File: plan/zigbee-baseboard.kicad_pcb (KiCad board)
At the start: 4 copper layers, 0 parts

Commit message: Initially update board from schematic
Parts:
- added AE1: 2450AT18A0100001E, Smarthome:Antenna_Johanson_2450AT18A0100001E, F.Cu at (128.1, 104.3)
- added C1: 2,3 pF, Capacitor_SMD:C_0201_0603Metric, F.Cu at (126.7, 98.1)
- added C101: 100 nF, Capacitor_SMD:C_0402_1005Metric, F.Cu at (126.9, 80.5)
- added C102: 10 µF, Capacitor_SMD:C_0603_1608Metric, F.Cu at (130.4, 86.0)
- added C103: 4,7 µF, Capacitor_SMD:C_0603_1608Metric, F.Cu at (130.4, 88.5)
- added C104: 1 µF, Capacitor_SMD:C_0402_1005Metric, F.Cu at (126.9, 82.5)
- added C105: 1 µF, Capacitor_SMD:C_0402_1005Metric, F.Cu at (126.9, 84.4)
- added C106: 1 µF, Capacitor_SMD:C_0402_1005Metric, F.Cu at (126.9, 86.4)
- added C107: 18 pF, Capacitor_SMD:C_0201_0603Metric, F.Cu at (129.6, 80.4)
- added C108: 0,5 pF, Capacitor_SMD:C_0201_0603Metric, F.Cu at (129.6, 82.1)
- added C109: 1 µF, Capacitor_SMD:C_0402_1005Metric, F.Cu at (126.9, 88.4)
- added C110: 1 µF, Capacitor_SMD:C_0402_1005Metric, F.Cu at (126.9, 90.3)
- added C111: 100 nF, Capacitor_SMD:C_0402_1005Metric, F.Cu at (126.9, 92.3)
- added C112: 100 nF, Capacitor_SMD:C_0402_1005Metric, F.Cu at (126.9, 94.3)
- added C2: 1,6 pF, Capacitor_SMD:C_0201_0603Metric, F.Cu at (126.7, 99.9)
- added C3: 0,3 pF, Capacitor_SMD:C_0201_0603Metric, F.Cu at (126.7, 101.6)
- added C4: TUNE, Capacitor_SMD:C_0201_0603Metric, F.Cu at (129.2, 98.1)
- added C5: TUNE, Capacitor_SMD:C_0201_0603Metric, F.Cu at (129.2, 99.9)
- added CC1: 0 Ω, Resistor_SMD:R_0201_0603Metric, F.Cu at (129.2, 101.6)
- added D1: APT1608LZGCK, LED_SMD:LED_0603_1608Metric, F.Cu at (143.0, 101.5)
- added FB101: 70 Ω @ 100 MHz, Inductor_SMD:L_0201_0603Metric, F.Cu at (129.6, 83.9)
- added J1: Debug_SWD_Pogo_2x3, Smarthome:Debug_SWD_Pogo_2x3_P2.00mm, F.Cu at (138.5, 102.6)
- added J2: EFR32MG24_Core_Expansion_2x6, Smarthome:Module_EFR32MG24_Core_Castellated_2x6_PTH_P2.54mm, F.Cu at (136.8, 87.2)
- added L1: 2,9 nH, Inductor_SMD:L_0201_0603Metric, F.Cu at (131.6, 98.1)
- added L101: DFE2HCAH2R2MJ0, Smarthome:Inductor_Murata_DFE2HCAH_2520, F.Cu at (130.6, 91.6)
- added L2: 1,2 nH, Inductor_SMD:L_0201_0603Metric, F.Cu at (131.6, 99.9)
- added L3: TUNE, Inductor_SMD:L_0201_0603Metric, F.Cu at (131.6, 101.6)
- added R1: 2.2 kΩ, 1%, Resistor_SMD:R_0402_1005Metric, F.Cu at (142.4, 103.8)
- added R101: 0 Ω, Resistor_SMD:R_0402_1005Metric, F.Cu at (132.3, 80.5)
- added R102: 0 Ω, Resistor_SMD:R_0402_1005Metric, F.Cu at (132.3, 82.5)
- added SW1: EVPBB2A9B000, Smarthome:Button_Panasonic_EVPBB_2.6x1.6mm, F.Cu at (143.3, 98.7)
- added TP1: GPIO_SolderPad, Smarthome:GPIO_SolderPad_D1.0mm_Bottom, F.Cu at (155.1, 80.8)
- added TP10: GPIO_SolderPad, Smarthome:GPIO_SolderPad_D1.0mm_Bottom, F.Cu at (157.7, 88.4)
- added TP11: GPIO_SolderPad, Smarthome:GPIO_SolderPad_D1.0mm_Bottom, F.Cu at (157.7, 91.0)
- added TP12: GPIO_SolderPad, Smarthome:GPIO_SolderPad_D1.0mm_Bottom, F.Cu at (157.7, 93.5)
- added TP13: GPIO_SolderPad, Smarthome:GPIO_SolderPad_D1.0mm_Bottom, F.Cu at (160.2, 80.8)
- added TP14: GPIO_SolderPad, Smarthome:GPIO_SolderPad_D1.0mm_Bottom, F.Cu at (160.2, 83.3)
- added TP15: GPIO_SolderPad, Smarthome:GPIO_SolderPad_D1.0mm_Bottom, F.Cu at (160.2, 85.9)
- added TP16: GPIO_SolderPad, Smarthome:GPIO_SolderPad_D1.0mm_Bottom, F.Cu at (160.2, 88.4)
- added TP17: GPIO_SolderPad, Smarthome:GPIO_SolderPad_D1.0mm_Bottom, F.Cu at (160.2, 91.0)
- added TP18: GPIO_SolderPad, Smarthome:GPIO_SolderPad_D1.0mm_Bottom, F.Cu at (160.2, 93.5)
- added TP19: GPIO_SolderPad, Smarthome:GPIO_SolderPad_D1.0mm_Bottom, F.Cu at (162.8, 80.8)
- added TP2: GPIO_SolderPad, Smarthome:GPIO_SolderPad_D1.0mm_Bottom, F.Cu at (155.1, 83.3)
- added TP20: GPIO_SolderPad, Smarthome:GPIO_SolderPad_D1.0mm_Bottom, F.Cu at (162.8, 83.3)
- added TP21: GPIO_SolderPad, Smarthome:GPIO_SolderPad_D1.0mm_Bottom, F.Cu at (162.8, 85.9)
- added TP22: GPIO_SolderPad, Smarthome:GPIO_SolderPad_D1.0mm_Bottom, F.Cu at (162.8, 88.4)
- added TP3: GPIO_SolderPad, Smarthome:GPIO_SolderPad_D1.0mm_Bottom, F.Cu at (155.1, 85.9)
- added TP4: GPIO_SolderPad, Smarthome:GPIO_SolderPad_D1.0mm_Bottom, F.Cu at (155.1, 88.4)
- added TP5: GPIO_SolderPad, Smarthome:GPIO_SolderPad_D1.0mm_Bottom, F.Cu at (155.1, 91.0)
- added TP6: GPIO_SolderPad, Smarthome:GPIO_SolderPad_D1.0mm_Bottom, F.Cu at (155.1, 93.5)
- added TP7: GPIO_SolderPad, Smarthome:GPIO_SolderPad_D1.0mm_Bottom, F.Cu at (157.7, 80.8)
- added TP8: GPIO_SolderPad, Smarthome:GPIO_SolderPad_D1.0mm_Bottom, F.Cu at (157.7, 83.3)
- added TP9: GPIO_SolderPad, Smarthome:GPIO_SolderPad_D1.0mm_Bottom, F.Cu at (157.7, 85.9)
- added U1: EFR32MG24B020F1536IM48-B, Smarthome:QFN-48-1EP_6x6mm_P0.4mm_EFR32MG24, F.Cu at (152.0, 101.1)
- added Y1: XTL501250-S315-038, Smarthome:Crystal_Siward_XTL501250_2.0x1.6mm, F.Cu at (149.6, 107.1)

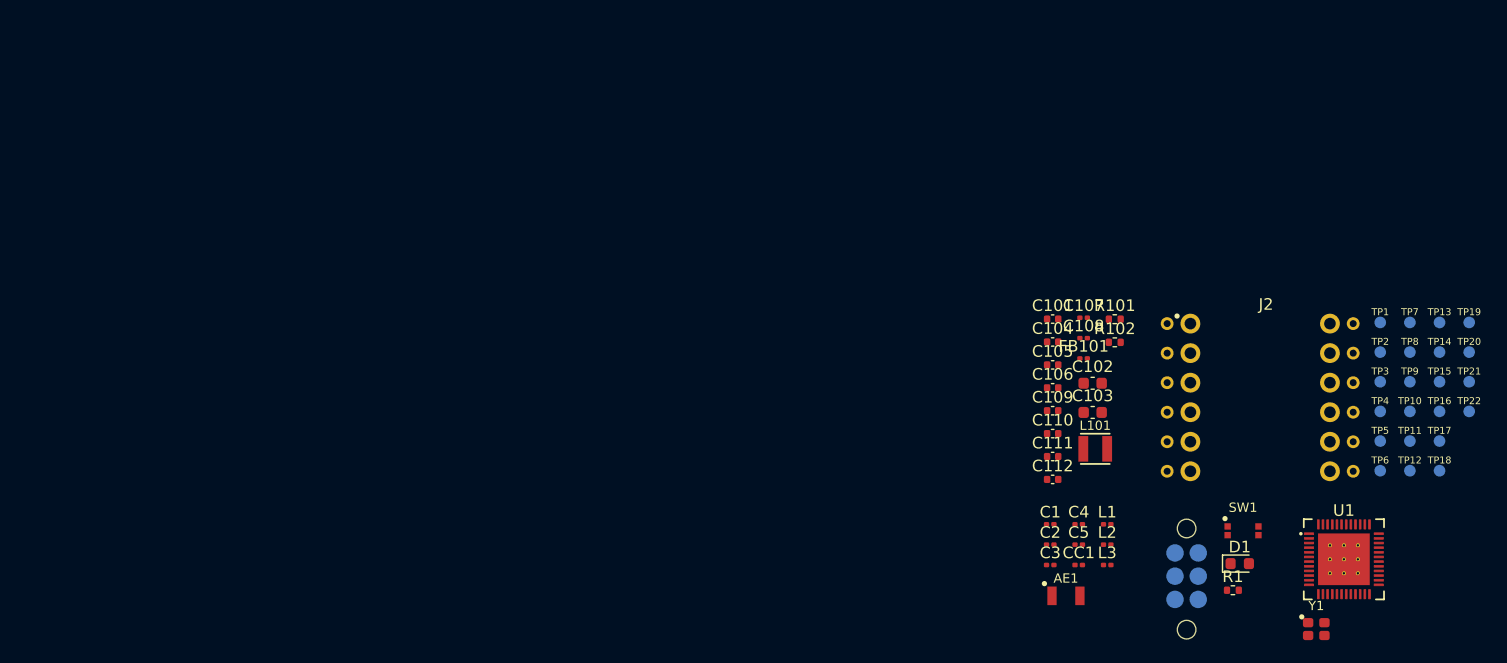
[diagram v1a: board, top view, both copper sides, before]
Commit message: First raw placement of RF-Block
- RF-Matching-Network
- Antenna-Tuning-Network
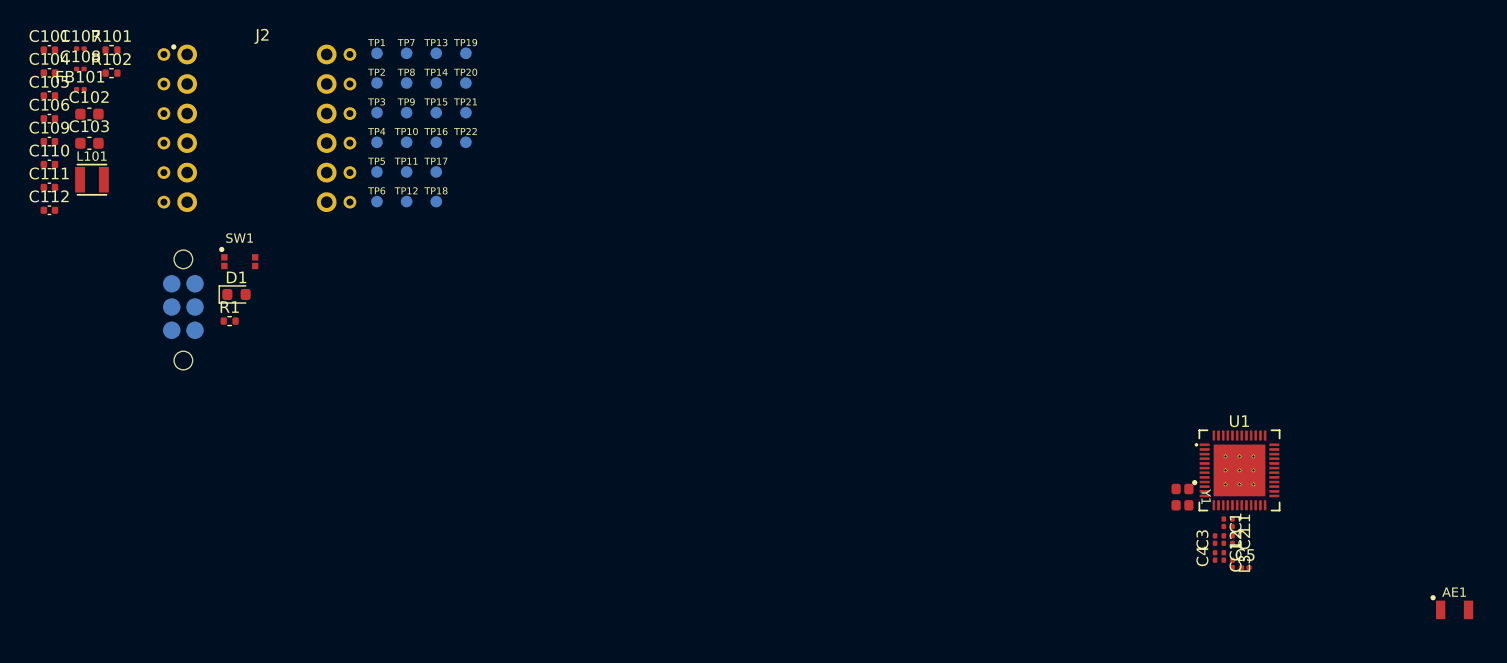
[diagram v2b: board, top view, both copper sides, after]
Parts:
- moved J1 89.3 mm to (52.2, 79.5)
- moved TP13 89.3 mm to (73.9, 57.6)
- moved TP14 89.3 mm to (73.9, 60.2)
- moved TP15 89.3 mm to (73.9, 62.7)
- moved TP16 89.3 mm to (73.9, 65.3)
- moved TP17 89.3 mm to (73.9, 67.8)
- moved TP18 89.3 mm to (73.9, 70.4)
- moved C101 89.3 mm to (40.7, 57.3)
- moved C102 89.3 mm to (44.1, 62.9)
- moved C103 89.3 mm to (44.1, 65.4)
- moved C104 89.3 mm to (40.7, 59.3)
- moved C105 89.3 mm to (40.7, 61.3)
- moved C106 89.3 mm to (40.7, 63.2)
- moved C107 89.3 mm to (43.3, 57.2)
- moved C108 89.3 mm to (43.3, 59.0)
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
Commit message: First raw placement of Power-Section
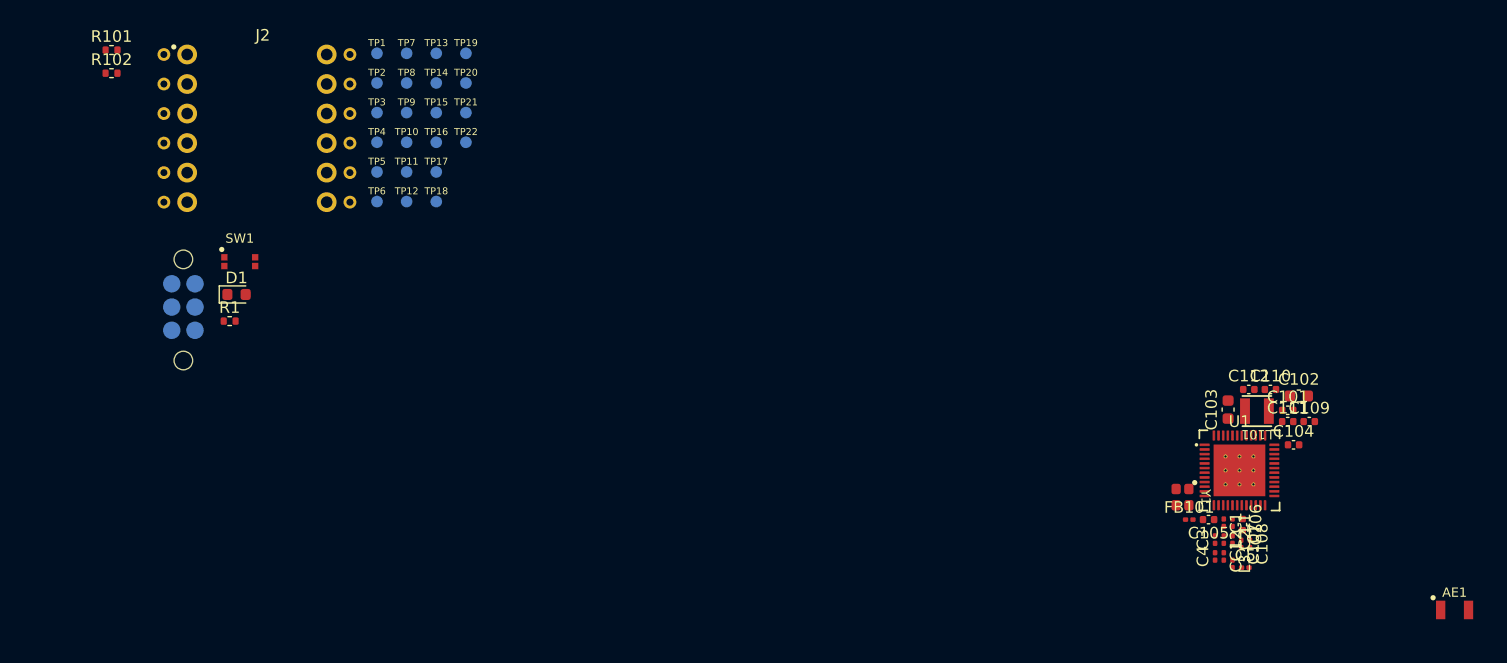
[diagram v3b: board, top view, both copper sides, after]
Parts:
- moved C104 111.7 mm to (147.7, 91.3)
- moved C109 111.0 mm to (149.0, 89.3)
- moved C101 110.9 mm to (147.2, 88.3)
- moved C108 108.6 mm to (143.9, 99.8), turned to -90 degrees
- moved C107 108.5 mm to (143.2, 99.8), turned to -90 degrees
- moved C111 108.4 mm to (147.2, 89.3)
- moved C106 108.4 mm to (143.2, 98.2), turned to -90 degrees
- moved C102 106.8 mm to (148.1, 87.1)
- moved C110 106.8 mm to (145.7, 86.5)
- moved C105 106.1 mm to (140.3, 97.7), turned to 180 degrees
- moved C112 104.3 mm to (143.8, 86.5)
- moved FB101 102.3 mm to (138.7, 97.7)
- moved L101 102.1 mm to (144.5, 88.4), turned to 180 degrees
- moved C103 100.6 mm to (142.0, 88.3), turned to 90 degrees

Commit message: Place antenna
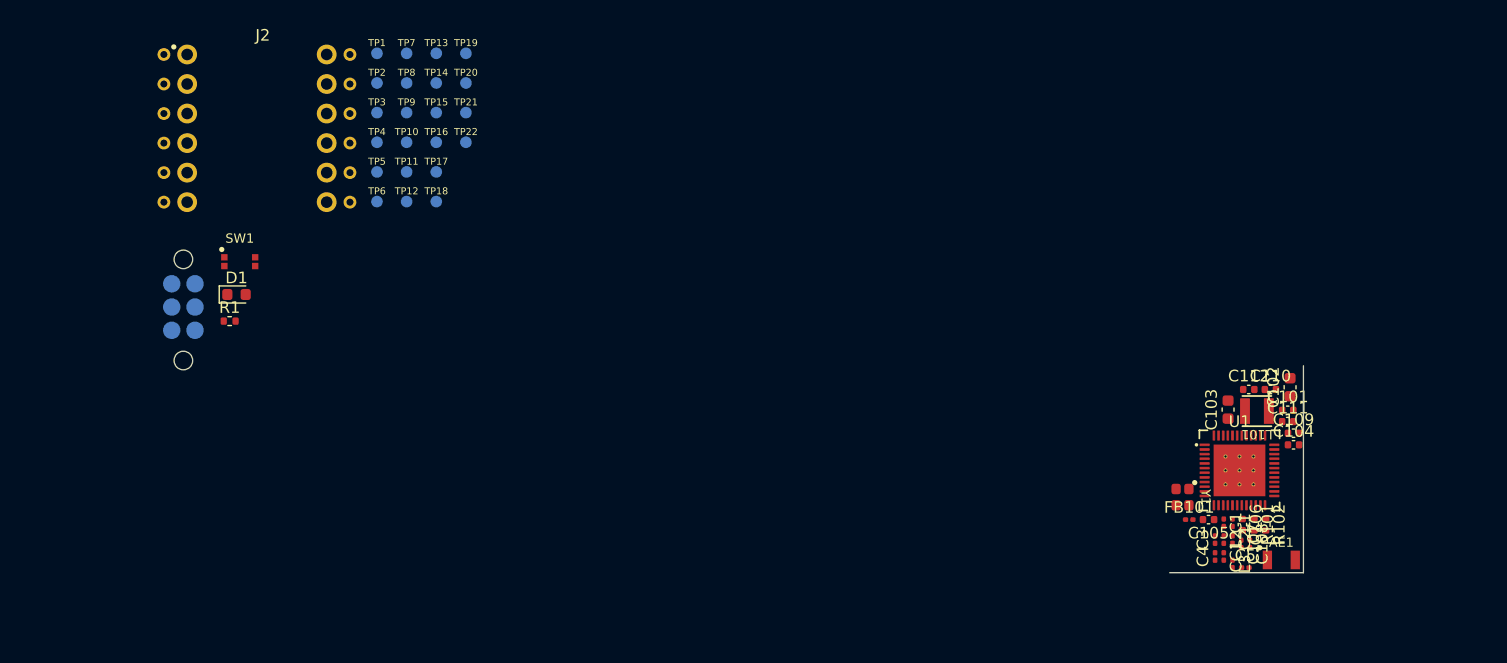
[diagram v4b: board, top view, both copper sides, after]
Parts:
- moved R102 106.6 mm to (145.2, 98.2), turned to -90 degrees
- moved R101 106.4 mm to (144.2, 98.2), turned to -90 degrees
- moved AE1 15.5 mm to (146.6, 101.2)
- moved C109 1.68 mm to (147.7, 90.3)
- moved C102 1.06 mm to (147.3, 86.3), turned to 90 degrees
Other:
- board outline added: 11.5 x 17.8 mm
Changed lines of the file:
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@@
 		(capping no)
 		(filling no)
-		(zone_defaults)
 		(pcbplotparams
 			(layerselection 0x00000000_00000000_55555555_5755f5ff)
@@
 	)
 	(footprint "Capacitor_SMD:C_0402_1005Metric"
+		(locked yes)
 		(layer "F.Cu")
 		(at 147.65 91.3)
@@
 	(footprint "Resistor_SMD:R_0402_1005Metric"
 		(layer "F.Cu")
-		(at 45.995 59.34)
+		(at 145.25 98.16 -90)
 		(descr "Resistor SMD 0402 (1005 Metric), square (rectangular) end terminal, IPC-7351 nominal, (Body size source: IPC-SM-782 page 72, https://www.pcb-3d.com/wordpress/wp-content/uploads/ipc-sm-782a_amendment_1_and_2.pdf)")
 		(tags "resistor")
 		(property "Reference" "R102"
-			(at 0 -1.17 0)
+			(at 0 -1.17 90)
 			(layer "F.SilkS")
 			(effects
@@
 		)
 		(property "Value" "0 Ω"
-			(at 0 1.17 0)
+			(at 0 1.17 90)
 			(layer "F.Fab")
 			(effects
@@
 		)
 		(property "Datasheet" ""
-			(at 0 0 0)
+			(at 0 0 90)
 			(layer "F.Fab")
 			(hide yes)
@@
 		)
 		(property "Description" "Resistor"
-			(at 0 0 0)
+			(at 0 0 90)
 			(layer "F.Fab")
 			(hide yes)
@@
 		)
 		(property "KiLib_Generator" "SMD_2terminal_chip_molded"
-			(at 0 0 0)
+			(at 0 0 90)
 			(layer "F.SilkS")
 			(hide yes)
@@
 		(duplicate_pad_numbers_are_jumpers no)
 		(fp_line
-			(start -0.153641 -0.38)
-			(end 0.153641 -0.38)
+			(start -0.153641 0.38)
+			(end 0.153641 0.38)
 			(stroke
 				(width 0.12)
@@
 		)
 		(fp_line
-			(start -0.153641 0.38)
-			(end 0.153641 0.38)
+			(start -0.153641 -0.38)
+			(end 0.153641 -0.38)
 			(stroke
 				(width 0.12)
@@
 		)
 		(fp_text user "${REFERENCE}"
-			(at 0 0 0)
+			(at 0 0 90)
 			(layer "F.Fab")
 			(effects
@@
 		)
 		(pad "1" smd roundrect
-			(at -0.51 0)
+			(at -0.51 0 270)
 			(size 0.54 0.64)
 			(layers "F.Cu" "F.Mask" "F.Paste")
@@
 		)
 		(pad "2" smd roundrect
-			(at 0.51 0)
+			(at 0.51 0 270)
 			(size 0.54 0.64)
 			(layers "F.Cu" "F.Mask" "F.Paste")
@@
 		(locked yes)
 		(layer "F.Cu")
-		(at 148.1 87.1)
+		(at 147.35 86.35 90)
 		(descr "Capacitor SMD 0603 (1608 Metric), square (rectangular) end terminal, IPC-7351 nominal, (Body size source: IPC-SM-782 page 76, https://www.pcb-3d.com/wordpress/wp-content/uploads/ipc-sm-782a_amendment_1_and_2.pdf)")
 		(tags "capacitor")
 		(property "Reference" "C102"
-			(at 0 -1.43 0)
+			(at 0 -1.43 90)
 			(layer "F.SilkS")
 			(effects
@@
 		)
 		(property "Value" "10 µF"
-			(at 0 1.43 0)
+			(at 0 1.43 90)
 			(layer "F.Fab")
 			(effects
@@
 		)
 		(property "Datasheet" ""
-			(at 0 0 0)
+			(at 0 0 90)
 			(layer "F.Fab")
 			(hide yes)
@@
 		)
 		(property "Description" "Polarized capacitor"
-			(at 0 0 0)
+			(at 0 0 90)
 			(layer "F.Fab")
 			(hide yes)
@@
 		)
 		(property "KiLib_Generator" "SMD_2terminal_chip_molded"
-			(at 0 0 0)
+			(at 0 0 90)
 			(layer "F.SilkS")
 			(hide yes)
@@
 		)
 		(fp_text user "${REFERENCE}"
-			(at 0 0 0)
+			(at 0 0 90)
 			(layer "F.Fab")
 			(effects
@@
 		)
 		(pad "1" smd roundrect
-			(at -0.775 0)
+			(at -0.775 0 90)
 			(size 0.9 0.95)
 			(layers "F.Cu" "F.Mask" "F.Paste")
@@
 		)
 		(pad "2" smd roundrect
-			(at 0.775 0)
+			(at 0.775 0 90)
 			(size 0.9 0.95)
 			(layers "F.Cu" "F.Mask" "F.Paste")
@@
 	(footprint "Smarthome:Antenna_Johanson_2450AT18A0100001E"
 		(layer "F.Cu")
-		(at 161.5 105.5)
+		(at 146.6 101.2)
 		(property "Reference" "AE1"
 			(at 0 -1.5 0)
@@
 		(locked yes)
 		(layer "F.Cu")
-		(at 149 89.3)
+		(at 147.65 90.3)
 		(descr "Capacitor SMD 0402 (1005 Metric), square (rectangular) end terminal, IPC-7351 nominal, (Body size source: IPC-SM-782 page 76, https://www.pcb-3d.com/wordpress/wp-content/uploads/ipc-sm-782a_amendment_1_and_2.pdf)")
 		(tags "capacitor")
@@
 	(footprint "Resistor_SMD:R_0402_1005Metric"
 		(layer "F.Cu")
-		(at 45.995 57.35)
+		(at 144.25 98.16 -90)
 		(descr "Resistor SMD 0402 (1005 Metric), square (rectangular) end terminal, IPC-7351 nominal, (Body size source: IPC-SM-782 page 72, https://www.pcb-3d.com/wordpress/wp-content/uploads/ipc-sm-782a_amendment_1_and_2.pdf)")
 		(tags "resistor")
 		(property "Reference" "R101"
-			(at 0 -1.17 0)
+			(at 0 -1.17 90)
 			(layer "F.SilkS")
 			(effects
@@
 		)
 		(property "Value" "0 Ω"
-			(at 0 1.17 0)
+			(at 0 1.17 90)
 			(layer "F.Fab")
 			(effects
@@
 		)
 		(property "Datasheet" ""
-			(at 0 0 0)
+			(at 0 0 90)
 			(layer "F.Fab")
 			(hide yes)
@@
 		)
 		(property "Description" "Resistor"
-			(at 0 0 0)
+			(at 0 0 90)
 			(layer "F.Fab")
 			(hide yes)
@@
 		)
 		(property "KiLib_Generator" "SMD_2terminal_chip_molded"
-			(at 0 0 0)
+			(at 0 0 90)
 			(layer "F.SilkS")
 			(hide yes)
@@
 		(duplicate_pad_numbers_are_jumpers no)
 		(fp_line
-			(start -0.153641 -0.38)
-			(end 0.153641 -0.38)
+			(start -0.153641 0.38)
+			(end 0.153641 0.38)
 			(stroke
 				(width 0.12)
@@
 		)
 		(fp_line
-			(start -0.153641 0.38)
-			(end 0.153641 0.38)
+			(start -0.153641 -0.38)
+			(end 0.153641 -0.38)
 			(stroke
 				(width 0.12)
@@
 		)
 		(fp_text user "${REFERENCE}"
-			(at 0 0 0)
+			(at 0 0 90)
 			(layer "F.Fab")
 			(effects
@@
 		)
 		(pad "1" smd roundrect
-			(at -0.51 0)
+			(at -0.51 0 270)
 			(size 0.54 0.64)
 			(layers "F.Cu" "F.Mask" "F.Paste")
@@
 		)
 		(pad "2" smd roundrect
-			(at 0.51 0)
+			(at 0.51 0 270)
 			(size 0.54 0.64)
 			(layers "F.Cu" "F.Mask" "F.Paste")
@@
 		(embedded_fonts no)
 	)
+	(gr_rect
+		(start 142 98.3)
+		(end 148.5 102.3)
+		(stroke
+			(width 0.1)
+			(type default)
+		)
+		(fill no)
+		(layer "Dwgs.User")
+	)
+	(gr_line
+		(start 137 102.3)
+		(end 148.5 102.3)
+		(stroke
+			(width 0.05)
+			(type default)
+		)
+		(layer "Edge.Cuts")
+	)
+	(gr_line
+		(start 148.5 84.5)
+		(end 148.5 102.3)
+		(stroke
+			(width 0.05)
+			(type default)
+		)
+		(layer "Edge.Cuts")
+	)
 	(embedded_fonts no)
